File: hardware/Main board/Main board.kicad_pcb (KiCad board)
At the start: 2 copper layers, 237.8 x 92.5 mm, 109 parts, among them J1 Wind Direction, J10 Free Pins, J11 Nokia 5110 LCD, J12 3v3 in, J2 Wind Speed, J3 USB_B_Micro, J4 Micro_SD_Card, J5 Sensor board connector, J6 230V AC IN, J7 ISP programmer, J8 SPI1, J9 SPI2, Q1 IRLML2060, SW1 SW_Push, SW2 SW_SPST, SW3 SW_Push, SW4 SW_Push, SW5 Page Switch btn, U1 FT232RL, U2 MCP6042, U4 ATmega1284P-AU, U5 DS3231MZ, U6 ENC28J60, U7 USB6B1, U8 DRV5053, Y1 16MHZ

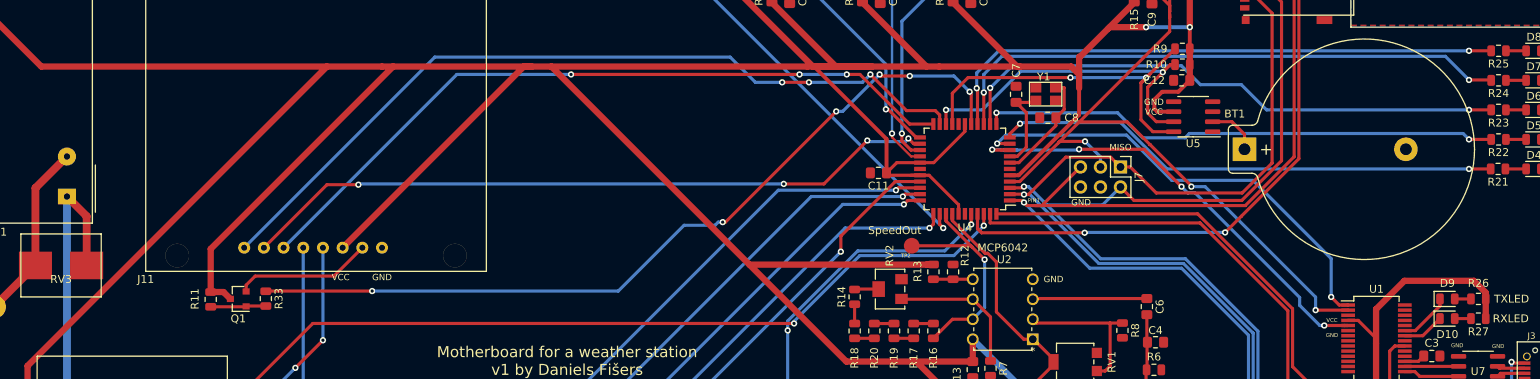
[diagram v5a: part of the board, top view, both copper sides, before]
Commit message: Changed a few pins
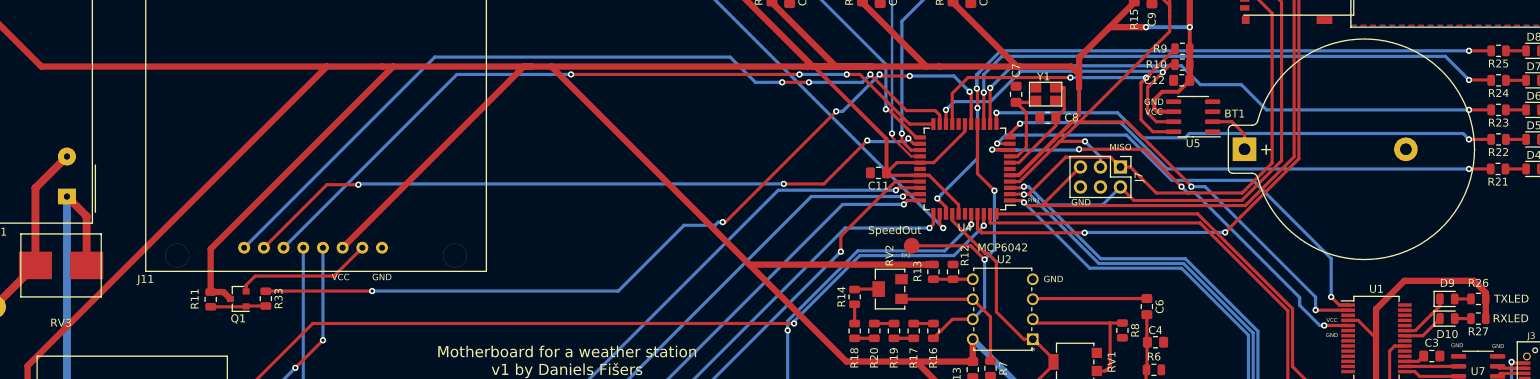
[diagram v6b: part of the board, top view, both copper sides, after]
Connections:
- R25 pad 2: Net-(R25-Pad2) -> PA1
- U4 pad 15: Net-(R25-Pad2) -> speedOUT
- U4 pad 36: speedOUT -> PA1
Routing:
- net PA1: track 0.00 -> 88.8 mm, vias 0 -> 4
- net Net-(R25-Pad2): track 73.0 -> 0.00 mm, vias 2 -> 0
- net speedOUT: track 29.7 -> 42.8 mm, vias 1 -> 2

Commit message: Slight improvements to the board
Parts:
- moved C26 50.8 mm to (87.0, 43.6), turned to 90 degrees
- moved C24 38.8 mm to (81.0, 43.6), turned to 90 degrees
- moved C10 30.7 mm to (77.0, 44.4), turned to 90 degrees
- moved RV3 27.4 mm to (41.8, 72.2), turned to 90 degrees
- moved R34 26.9 mm to (70.3, 45.4), turned to 0 degrees
- moved Q1 25.6 mm to (116.3, 83.1)
- moved R11 25.6 mm to (112.8, 83.2)
- moved R33 25.6 mm to (119.8, 83.1)
- moved D11 25.3 mm to (65.9, 45.4), turned to 0 degrees
- moved PS1 17.5 mm to (51.6, 69.0), turned to 90 degrees
- moved J11 10.8 mm to (89.8, 79.8)
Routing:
- net GND: track 0.56 -> 102.3 mm
- net VCC: track 909.6 -> 858.1 mm, vias 5 -> 6
- net PD7: track 105.8 -> 80.1 mm
- net PC2: track 103.3 -> 89.8 mm
- net Net-(J11-Pad7): track 17.5 -> 5.37 mm
- net Net-(F1-Pad2): track 22.9 -> 34.3 mm
- net PC5: track 89.4 -> 78.6 mm, vias 4 -> 3
- net PC3: track 94.2 -> 87.3 mm, vias 3 -> 4
- net MOSI: track 335.2 -> 339.3 mm
- net SCK: track 377.1 -> 380.8 mm, vias 3 -> 2
- net TXD: track 58.4 -> 55.6 mm
- net Net-(R22-Pad2): track 66.1 -> 68.8 mm
- net Net-(J6-Pad2): track 59.3 -> 61.0 mm
- net RST: track 110.5 -> 109.5 mm
- net Net-(R21-Pad2): track 64.5 -> 65.2 mm
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
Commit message: Slight adjustments
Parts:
- moved SW2 3.20 mm to (50.8, 101.2)
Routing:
- net Net-(J6-Pad1): track 18.2 -> 16.9 mm
- net Net-(F1-Pad1): track 23.7 -> 22.4 mm
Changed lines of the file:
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@@
     (thickness 1.6)
     (drawings 81)
-    (tracks 741)
+    (tracks 742)
     (zones 0)
     (modules 109)
@@
   )
   (module Meteo_Footprints:Switch_NEW (layer F.Cu)
-    (at 54 101.25 180)
+    (at 50.8 101.25 180)
     (fp_text reference SW2 (at 0 3.7) (layer F.SilkS)
       (effects (font (size 1 1) (thickness 0.15)))
@@
   (segment (start 246.2 105.5) (end 254 113.3) (width 0.4) (layer B.Cu) (net 40))
   (segment (start 238 105.5) (end 246.2 105.5) (width 0.4) (layer B.Cu) (net 40))
-  (segment (start 50.5 108.45) (end 57.7 101.25) (width 0.8) (layer F.Cu) (net 41))
-  (segment (start 50.5 116.5) (end 50.5 108.45) (width 0.8) (layer F.Cu) (net 41))
+  (segment (start 50.5 105.25) (end 54.5 101.25) (width 1) (layer F.Cu) (net 41))
+  (segment (start 50.5 116.5) (end 50.5 105.25) (width 1) (layer F.Cu) (net 41))
   (via (at 183.8 74.044028) (size 0.8) (drill 0.4) (layers F.Cu B.Cu) (net 43))
   (segment (start 183.8 72.7) (end 183.8 74.044028) (width 0.4) (layer F.Cu) (net 43) (status 10))
@@
   (segment (start 214.250001 68.449999) (end 214.349999 68.449999) (width 0.4) (layer B.Cu) (net 85))
   (segment (start 214.349999 68.449999) (end 229.4 83.5) (width 0.4) (layer B.Cu) (net 85))
-  (segment (start 230.875 83.5) (end 231.65 84.275) (width 0.4) (layer F.Cu) (net 85))
-  (segment (start 229.4 83.5) (end 230.875 83.5) (width 0.4) (layer F.Cu) (net 85))
+  (segment (start 230.175 84.275) (end 229.4 83.5) (width 0.4) (layer F.Cu) (net 85))
+  (segment (start 231.65 84.275) (end 230.175 84.275) (width 0.4) (layer F.Cu) (net 85))
   (via (at 185.4 74.2) (size 0.8) (drill 0.4) (layers F.Cu B.Cu) (net 86))
   (segment (start 185.4 72.7) (end 185.4 74.2) (width 0.4) (layer F.Cu) (net 86) (status 10))
@@
   (segment (start 50.23 75.45) (end 56.68 69) (width 1) (layer F.Cu) (net 98))
   (segment (start 41.8 75.45) (end 50.23 75.45) (width 1) (layer F.Cu) (net 98))
-  (segment (start 54 101.25) (end 37.25 84.5) (width 1) (layer F.Cu) (net 99))
+  (segment (start 50.8 98.05) (end 37.25 84.5) (width 1) (layer F.Cu) (net 99))
+  (segment (start 50.8 101.25) (end 50.8 98.05) (width 1) (layer F.Cu) (net 99))
   (segment (start 41.85 69) (end 41.8 68.95) (width 1) (layer F.Cu) (net 100))
   (segment (start 51.6 69) (end 41.85 69) (width 1) (layer F.Cu) (net 100))
@@
     (connect_pads (clearance 0.2))
     (min_thickness 0.2)
-    (fill (arc_segments 32) (thermal_gap 0.2) (thermal_bridge_width 0.508))
+    (fill yes (arc_segments 32) (thermal_gap 0.2) (thermal_bridge_width 0.508))
     (polygon
       (pts
@@
     (connect_pads (clearance 0.2))
     (min_thickness 0.2)
-    (fill (arc_segments 32) (thermal_gap 0.2) (thermal_bridge_width 0.508))
+    (fill yes (arc_segments 32) (thermal_gap 0.2) (thermal_bridge_width 0.508))
     (polygon
       (pts
